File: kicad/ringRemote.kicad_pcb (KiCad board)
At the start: 4 copper layers, 14.2 x 23 mm, 25 parts, among them Y1 32.768kHz

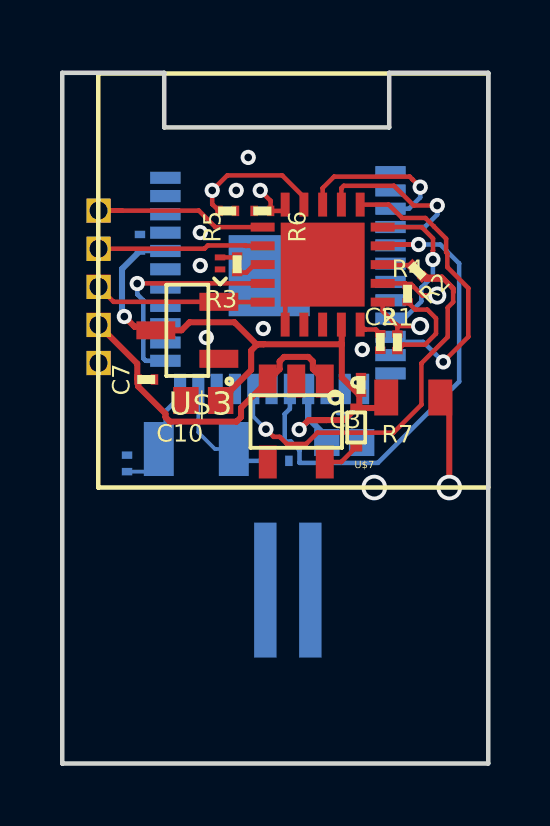
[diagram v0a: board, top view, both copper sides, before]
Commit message: had to wire GND castellation to polypour; the border technically isn't filled
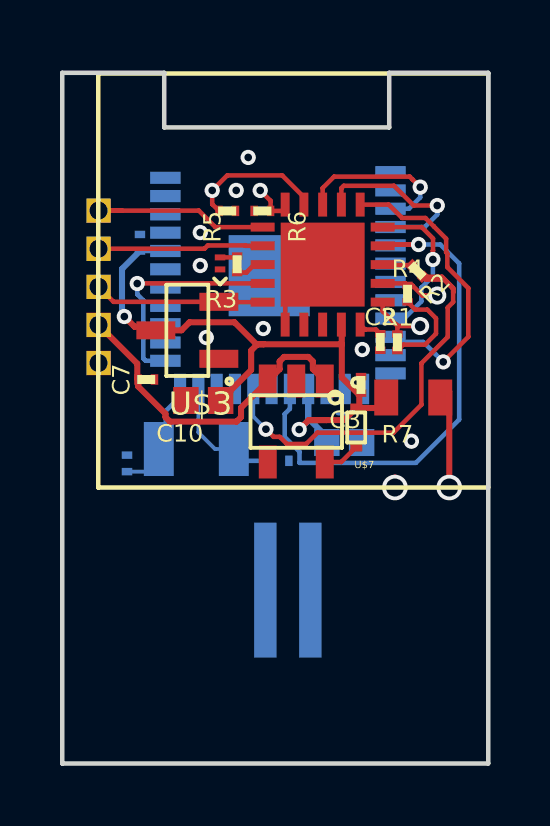
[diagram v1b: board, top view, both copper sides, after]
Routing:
- net /WAKEMONITOR: track 17.0 -> 17.7 mm
- net GND: track 6.59 -> 6.97 mm, vias 7 -> 9
- net 3.3V: vias 1 -> 0

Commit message: finished routing main board; changed programming castellations to circular; created subschematic for battery board
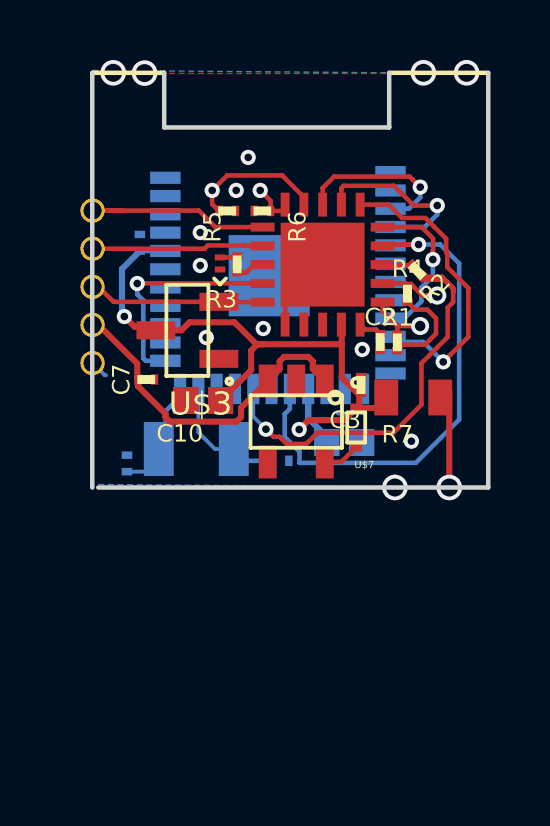
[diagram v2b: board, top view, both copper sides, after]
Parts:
- removed U$5: ML621S, ringRemote:ML621S
- moved U$6 0.20 mm to (142.4, 100.6)
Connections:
- R7 pad 1: /VBAT -> /battery/VBAT
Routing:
- net /battery/VBAT: track 0.00 -> 3.56 mm, vias 0 -> 1
- net /VBAT: track 3.56 -> 0.00 mm, vias 1 -> 0
- net /PB3: track 7.79 -> 10.4 mm, vias 1 -> 2
- net /PB4: track 5.81 -> 7.91 mm, vias 1 -> 2
- net /PB2: track 8.44 -> 9.97 mm, vias 1 -> 2
- net /PB1: track 10.6 -> 11.8 mm, vias 1 -> 2
- net GND: track 6.97 -> 7.59 mm
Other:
- board size 14.2 x 23 mm -> 13.2 x 13.8 mm

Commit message: added 4 pin spst switch and finished sch
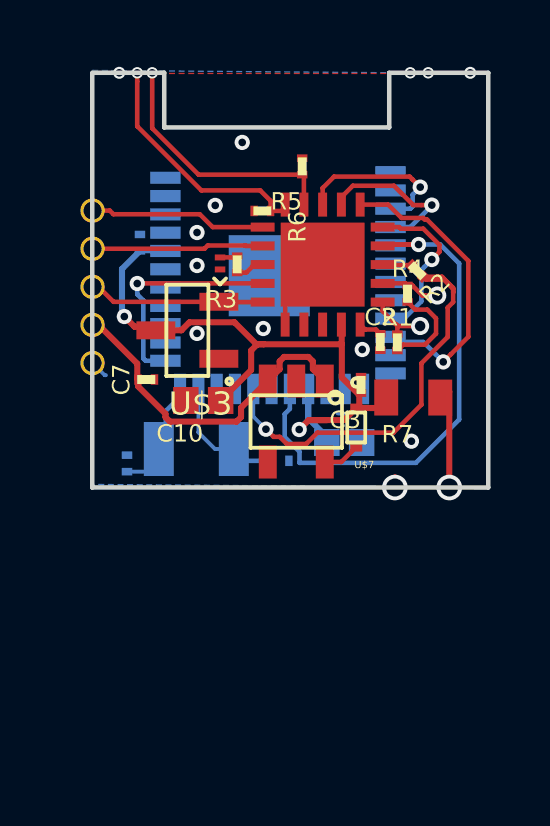
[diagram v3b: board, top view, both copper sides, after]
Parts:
- moved R5 2.91 mm to (149.4, 96.6), turned to 180 degrees
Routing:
- net VCC: track 25.7 -> 49.8 mm, vias 2 -> 4
- net /PB3: track 10.4 -> 9.06 mm, vias 2 -> 1
- net /BT_TXD: track 6.08 -> 5.38 mm
- net /SWDCLK: track 6.49 -> 5.90 mm
- net /PB4: track 7.91 -> 8.27 mm, vias 2 -> 1
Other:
- outline, holes or cut-outs redrawn

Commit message: fixed MAX32660 footprint (was actually wrong, design reviews are good), updated to board; slightly nudged pb4 via away from pb3 via (drc error)
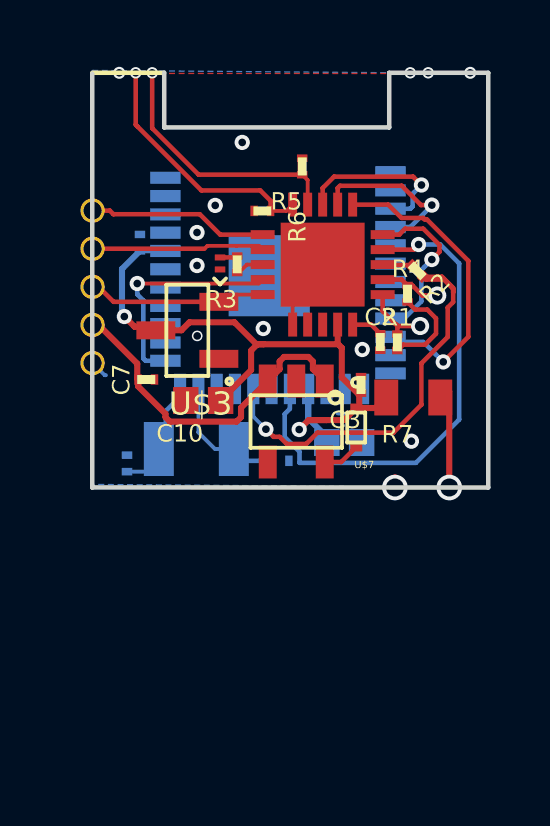
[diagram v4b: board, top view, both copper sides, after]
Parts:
- removed FRAME1: FRAME-LETTERNO_PACKAGE, ringRemote:DUMMY
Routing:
- net GND: track 7.61 -> 9.28 mm
- net /WAKEMONITOR: track 17.7 -> 16.7 mm
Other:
- net class Default: via_dia 0.508 -> 0.3556
- rule via_min_size: 0.4 -> 0.3556
